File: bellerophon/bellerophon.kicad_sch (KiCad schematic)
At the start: 44 parts, among them Q1 ST3413A, Q2 SPP3414S23RG, Q3 SPP3414S23RG, U1 HT7350-A, U2 BNO055, U3 MPL3115A2, U4 Teensy4.0, U5 XTSD, Y1 32.768kHz

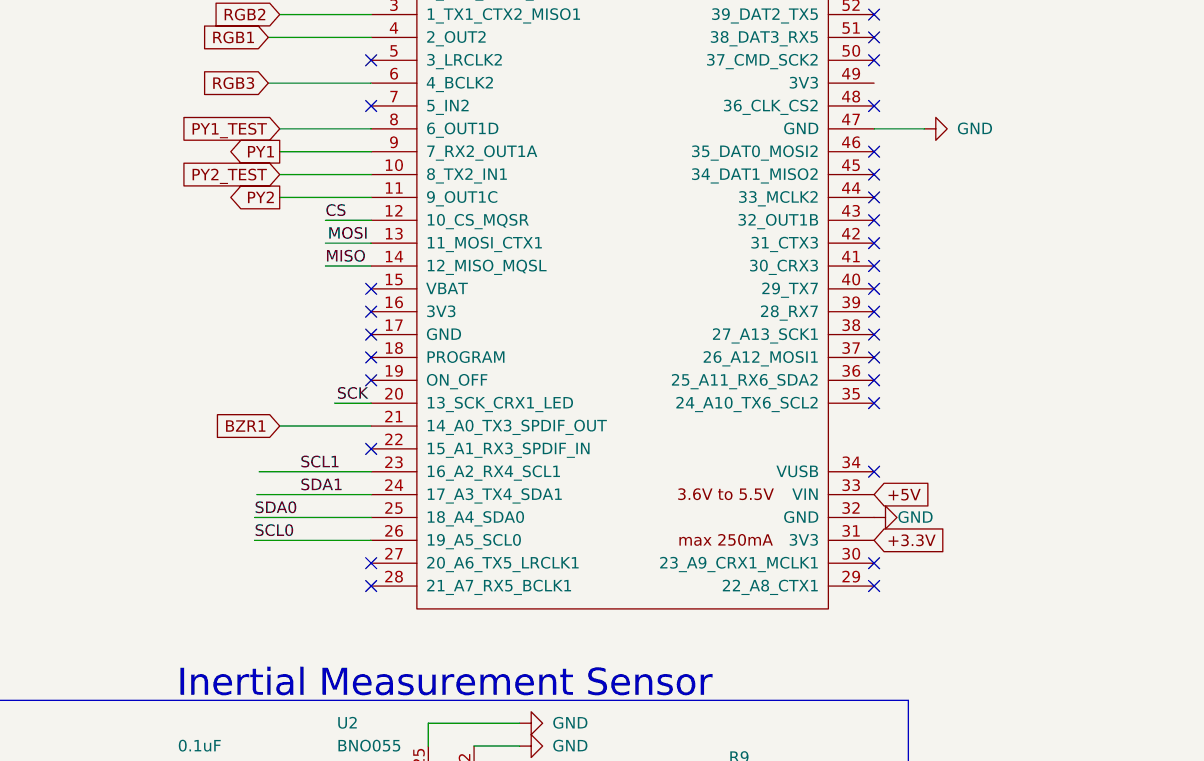
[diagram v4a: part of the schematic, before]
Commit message: route all signal traces
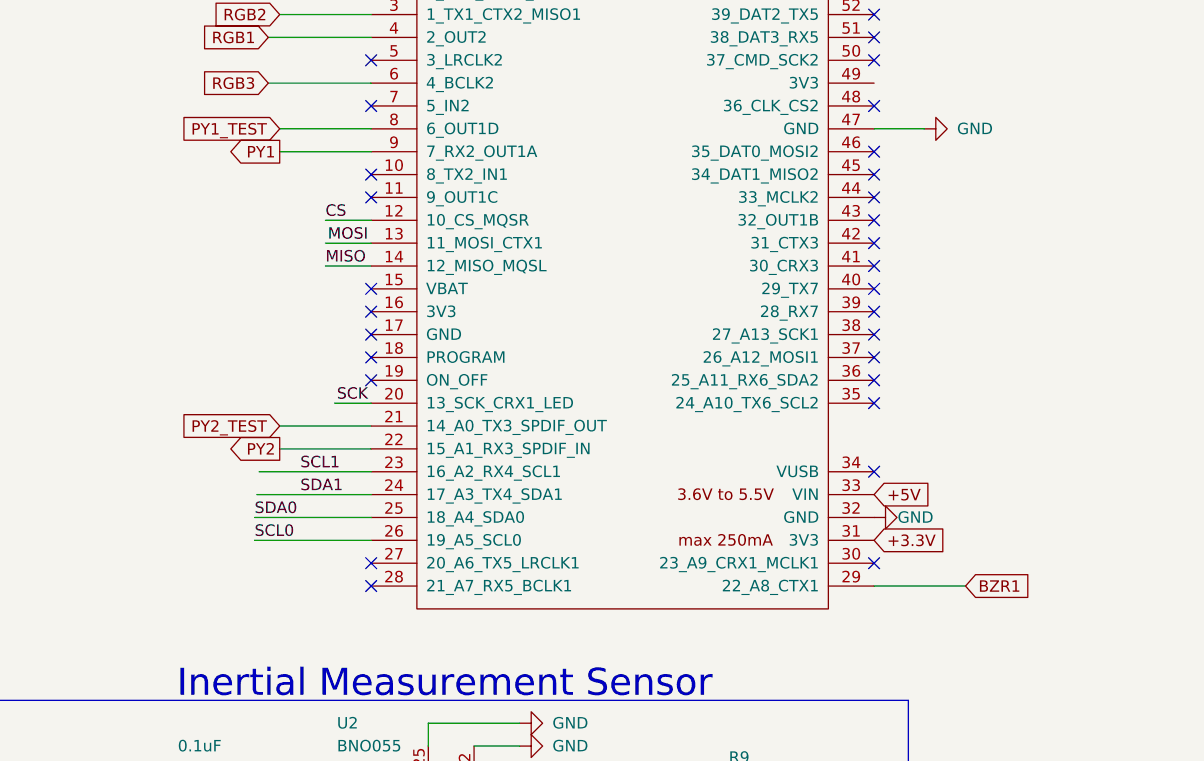
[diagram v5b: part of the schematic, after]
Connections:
- net BZR1: now also U4.29 (22_A8_CTX1); no longer U4.21 (14_A0_TX3_SPDIF_OUT)
- net PY2: now also U4.22 (15_A1_RX3_SPDIF_IN); no longer U4.11 (9_OUT1C)
- net PY2_TEST: now also U4.21 (14_A0_TX3_SPDIF_OUT); no longer U4.10 (8_TX2_IN1)
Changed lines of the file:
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@@
   )
   (no_connect (at 116.84 72.39))
-  (no_connect (at 116.84 123.19))
+  (no_connect (at 172.72 135.89))
   (no_connect (at 116.84 113.03))
   (no_connect (at 116.84 115.57))
@@
   (no_connect (at 172.72 72.39))
   (no_connect (at 172.72 69.85))
-  (no_connect (at 172.72 138.43))
-  (no_connect (at 172.72 135.89))
+  (no_connect (at 116.84 138.43))
+  (no_connect (at 116.84 135.89))
   (no_connect (at 172.72 125.73))
   (no_connect (at 172.72 118.11))
@@
   (no_connect (at 172.72 102.87))
   (no_connect (at 172.72 105.41))
-  (no_connect (at 116.84 135.89))
-  (no_connect (at 116.84 138.43))
+  (no_connect (at 116.84 92.71))
+  (no_connect (at 116.84 95.25))
   (no_connect (at 116.84 107.95))
   (no_connect (at 116.84 105.41))
@@
     (stroke (width 0) (type default) (color 0 0 0 0))
   )
-  (wire (pts (xy 106.68 92.71) (xy 116.84 92.71))
+  (wire (pts (xy 106.68 120.65) (xy 116.84 120.65))
     (stroke (width 0) (type default) (color 0 0 0 0))
   )
@@
     (stroke (width 0) (type default) (color 0 0 0 0))
   )
-  (wire (pts (xy 106.68 120.65) (xy 116.84 120.65))
+  (wire (pts (xy 182.88 138.43) (xy 172.72 138.43))
     (stroke (width 0) (type default) (color 0 0 0 0))
   )
@@
     (stroke (width 0) (type default) (color 0 0 0 0))
   )
-  (wire (pts (xy 106.68 95.25) (xy 116.84 95.25))
+  (wire (pts (xy 106.68 123.19) (xy 116.84 123.19))
     (stroke (width 0) (type default) (color 0 0 0 0))
   )
@@
     )
   )
-  (global_label "BZR1" (shape input) (at 106.68 120.65 180) (fields_autoplaced)
-    (effects (font (size 1.27 1.27)) (justify right))
-    (property "Intersheet References" "${INTERSHEET_REFS}" (id 0) (at 99.3079 120.5706 0)
-      (effects (font (size 1.27 1.27)) (justify right) hide)
+  (global_label "BZR1" (shape input) (at 182.88 138.43 0) (fields_autoplaced)
+    (effects (font (size 1.27 1.27)) (justify left))
+    (property "Intersheet References" "${INTERSHEET_REFS}" (id 0) (at 190.2521 138.5094 0)
+      (effects (font (size 1.27 1.27)) (justify left) hide)
     )
   )
@@
     )
   )
-  (global_label "PY2_TEST" (shape input) (at 106.68 92.71 180) (fields_autoplaced)
-    (effects (font (size 1.27 1.27)) (justify right))
-    (property "Intersheet References" "${INTERSHEET_REFS}" (id 0) (at 95.4374 92.6306 0)
+  (global_label "PY2_TEST" (shape input) (at 106.68 120.65 180) (fields_autoplaced)
+    (effects (font (size 1.27 1.27)) (justify right))
+    (property "Intersheet References" "${INTERSHEET_REFS}" (id 0) (at 95.4374 120.5706 0)
       (effects (font (size 1.27 1.27)) (justify right) hide)
     )
@@
     )
   )
-  (global_label "PY2" (shape output) (at 106.68 95.25 180) (fields_autoplaced)
-    (effects (font (size 1.27 1.27)) (justify right))
-    (property "Intersheet References" "${INTERSHEET_REFS}" (id 0) (at 100.6988 95.1706 0)
-      (effects (font (size 1.27 1.27)) (justify right) hide)
-    )
+  (global_label "PY2" (shape output) (at 106.68 123.19 180) (fields_autoplaced)
+    (effects (font (size 1.27 1.27)) (justify right))
+    (property "Intersheet References" "${INTERSHEET_REFS}" (id 0) (at 100.6988 123.1106 0)
+      (effects (font (size 1.27 1.27)) (justify right) hide)
+    )

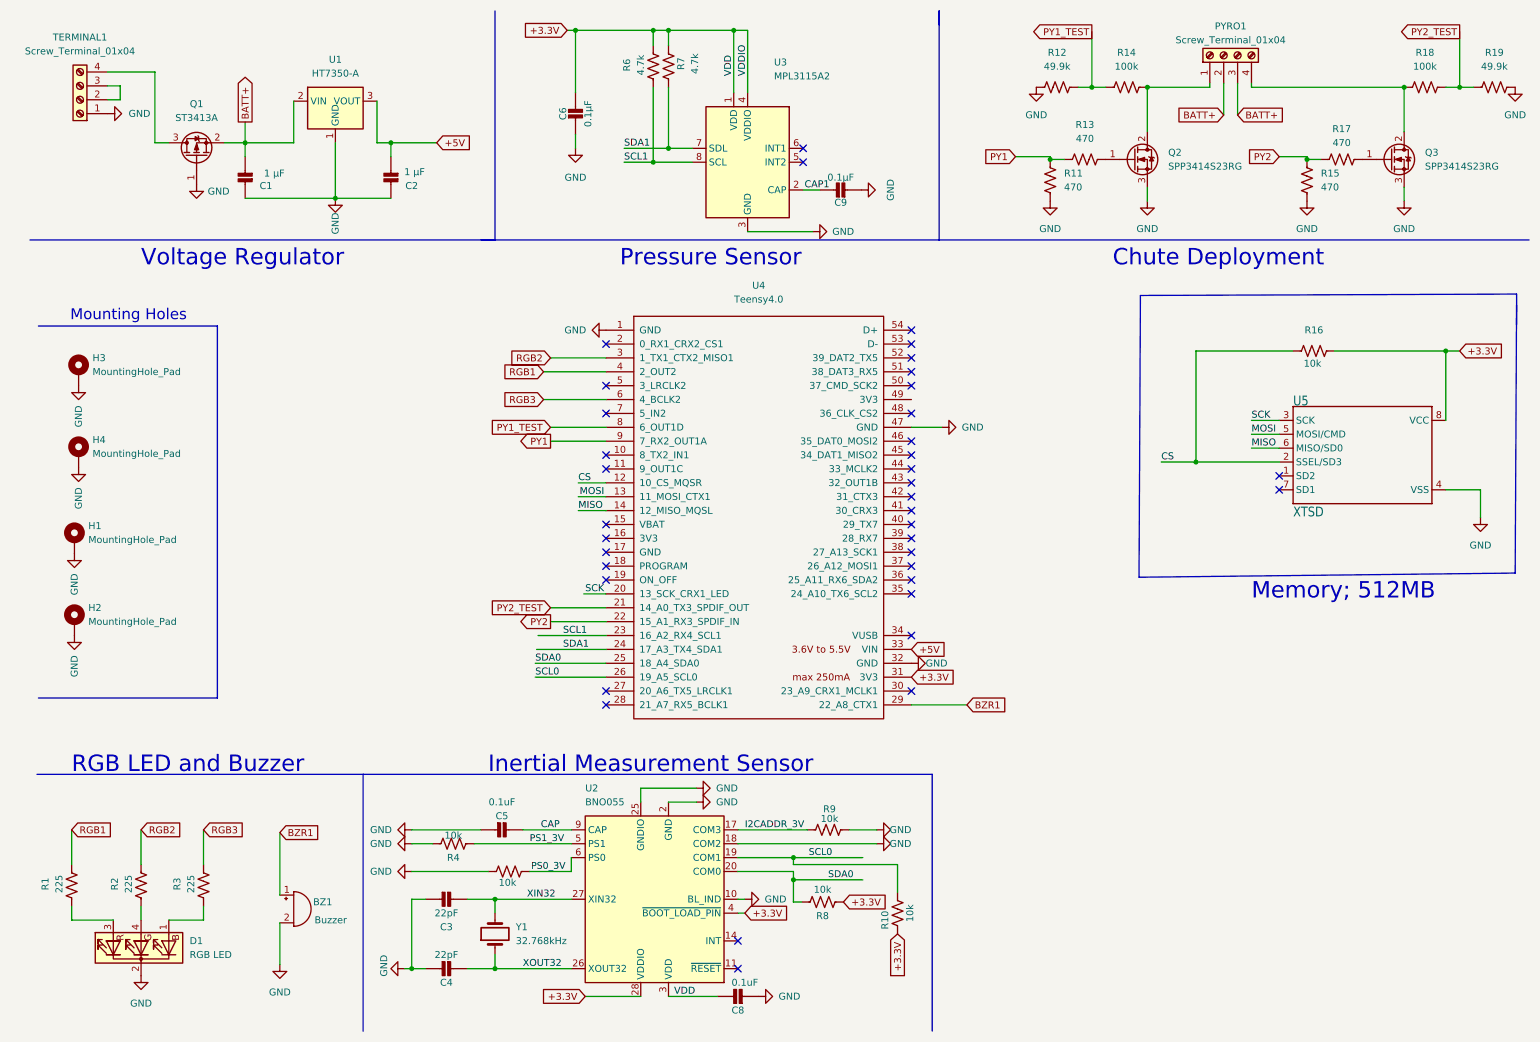
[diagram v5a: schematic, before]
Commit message: add 3 fiducials, move components to accomodate
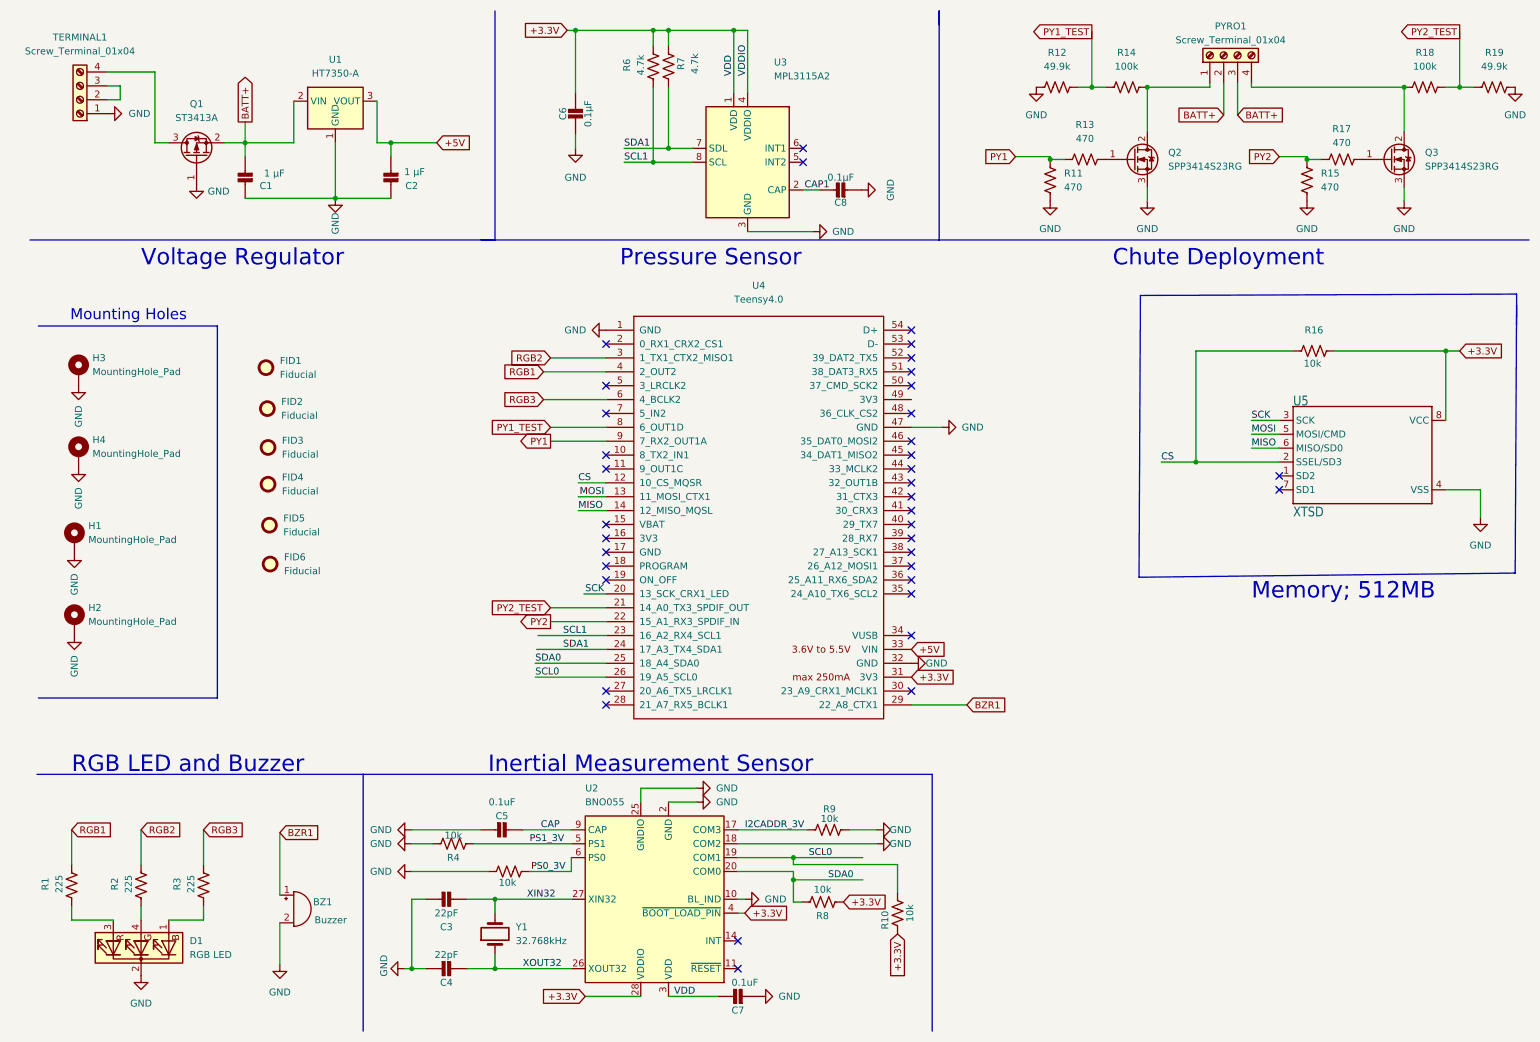
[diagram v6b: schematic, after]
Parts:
- added FID1, FID2, FID3, FID4, FID5, FID6: Fiducial, Fiducial:Fiducial_1mm_Mask2mm, symbol Mechanical:Fiducial
- renumbered C8 to C7, C9 to C8

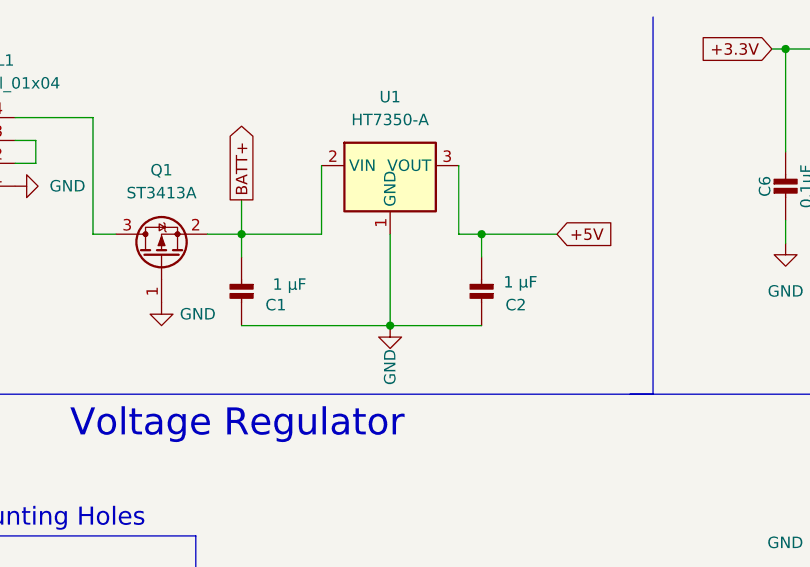
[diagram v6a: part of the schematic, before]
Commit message: extend board length to 37mm to comply with mounting regulations
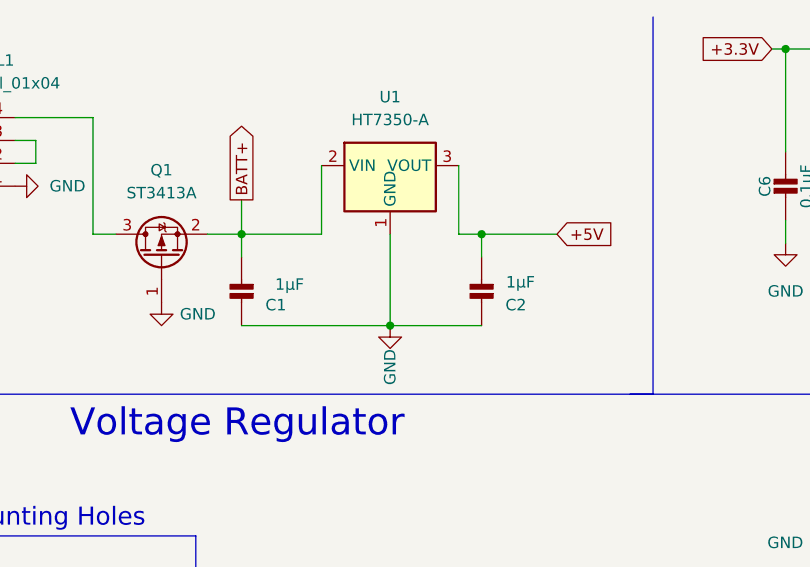
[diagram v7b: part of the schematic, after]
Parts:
- BZ1, D1, FID1, FID4, FID5, FID6, H1, H2, H3, H4, PYRO1, TERMINAL1, U4: now left out of the parts list
- C1, C2: value 1 µF -> 1µF
- R11, R12, R13, R14, R15, R17, R18, R19: footprint Resistor_SMD:R_1206_3216Metric_Pad1.30x1.75mm_HandSolder -> Resistor_SMD:R_1206_3216Metric
